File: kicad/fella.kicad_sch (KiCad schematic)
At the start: 4 parts

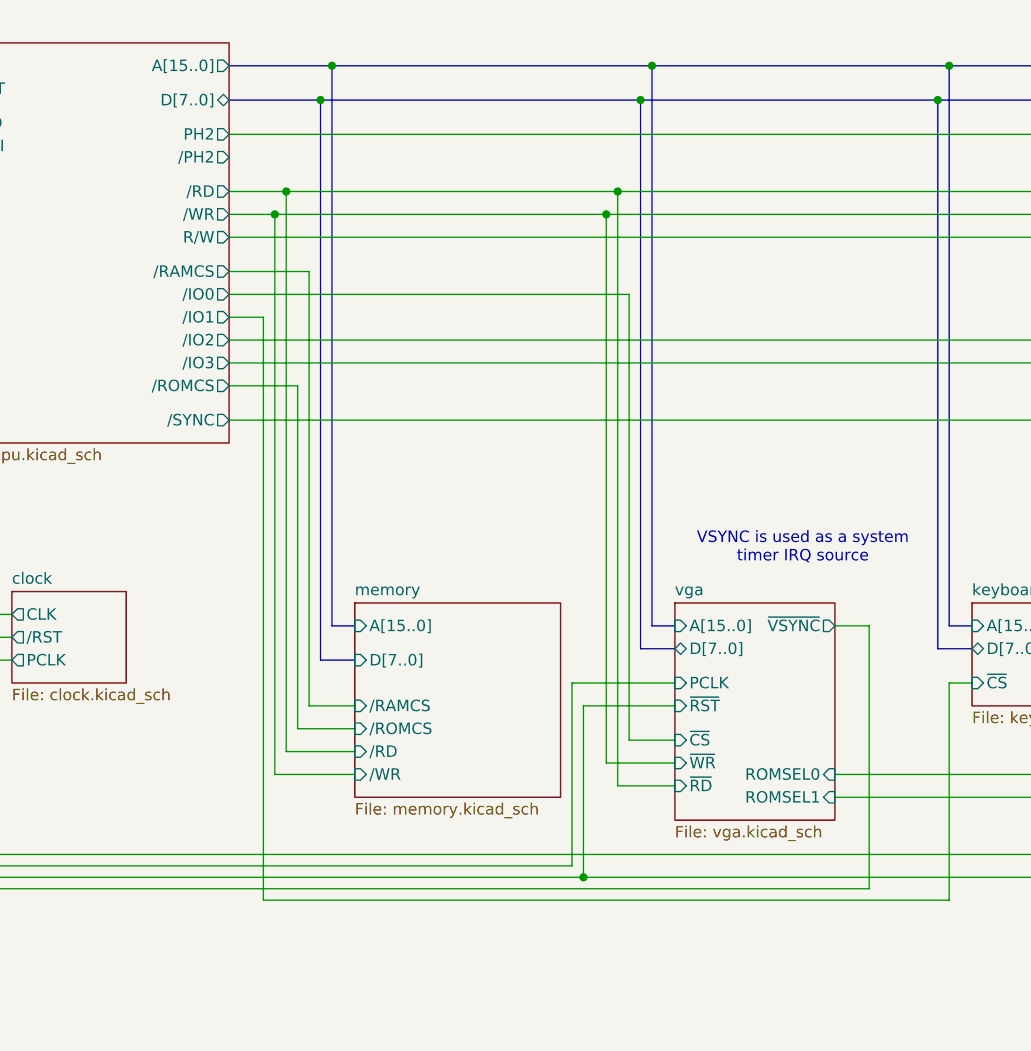
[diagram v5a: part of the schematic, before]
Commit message: hw: Start work on rev B
Changelog:
- fixed IO address decoder (removed /PH2 gating),
- added missing reset circuit capacitor,
- added hardware VGA scrolling,
- removed VGA column register, replaced with address bus,
- fixed values of R5 and R6.
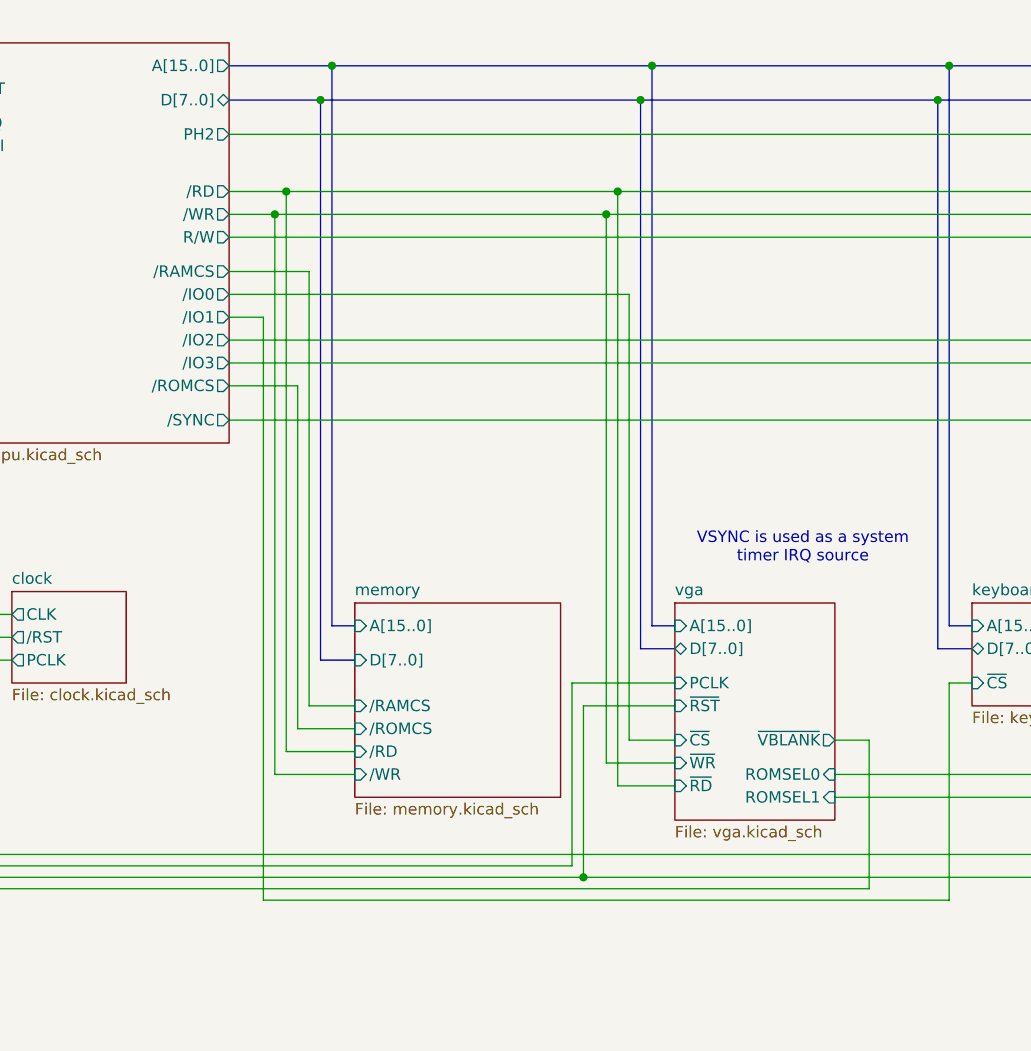
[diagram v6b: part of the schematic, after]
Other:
- sheet cpu ports: added none; removed /PH2
- sheet vga ports: added ~{VBLANK}; removed ~{VSYNC}
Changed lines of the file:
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@@
+	(wire
+		(pts
+			(xy 132.08 132.08) (xy 132.08 115.57)
+		)
+		(stroke
+			(width 0)
+			(type default)
+		)
+	)
 	(wire
 		(pts
@@
 	(wire
 		(pts
-			(xy 128.27 102.87) (xy 132.08 102.87)
-		)
-		(stroke
-			(width 0)
-			(type default)
-		)
-	)
-	(wire
-		(pts
 			(xy 67.31 54.61) (xy 67.31 116.84)
 		)
@@
 		)
 	)
+	(wire
+		(pts
+			(xy 132.08 115.57) (xy 128.27 115.57)
+		)
+		(stroke
+			(width 0)
+			(type default)
+		)
+	)
 	(bus
 		(pts
@@
 		(pts
 			(xy 110.49 102.87) (xy 107.95 102.87)
-		)
-		(stroke
-			(width 0)
-			(type default)
-		)
-	)
-	(wire
-		(pts
-			(xy 132.08 102.87) (xy 132.08 132.08)
 		)
 		(stroke
@@
 			)
 		)
-		(pin "~{VSYNC}" output
-			(at 128.27 102.87 0)
-			(effects
-				(font
-					(size 1.27 1.27)
-				)
-				(justify right)
-			)
-		)
 		(pin "ROMSEL1" input
 			(at 128.27 121.92 0)
@@
 		(pin "ROMSEL0" input
 			(at 128.27 119.38 0)
+			(effects
+				(font
+					(size 1.27 1.27)
+				)
+				(justify right)
+			)
+		)
+		(pin "~{VBLANK}" output
+			(at 128.27 115.57 0)
 			(effects
 				(font
@@
 			(effects
 				(font
-					(size 1.27 1.27)
-				)
-				(justify right)
-			)
-		)
-		(pin "{slash}PH2" output
-			(at 60.96 50.8 0)
-			(effects
-				(font

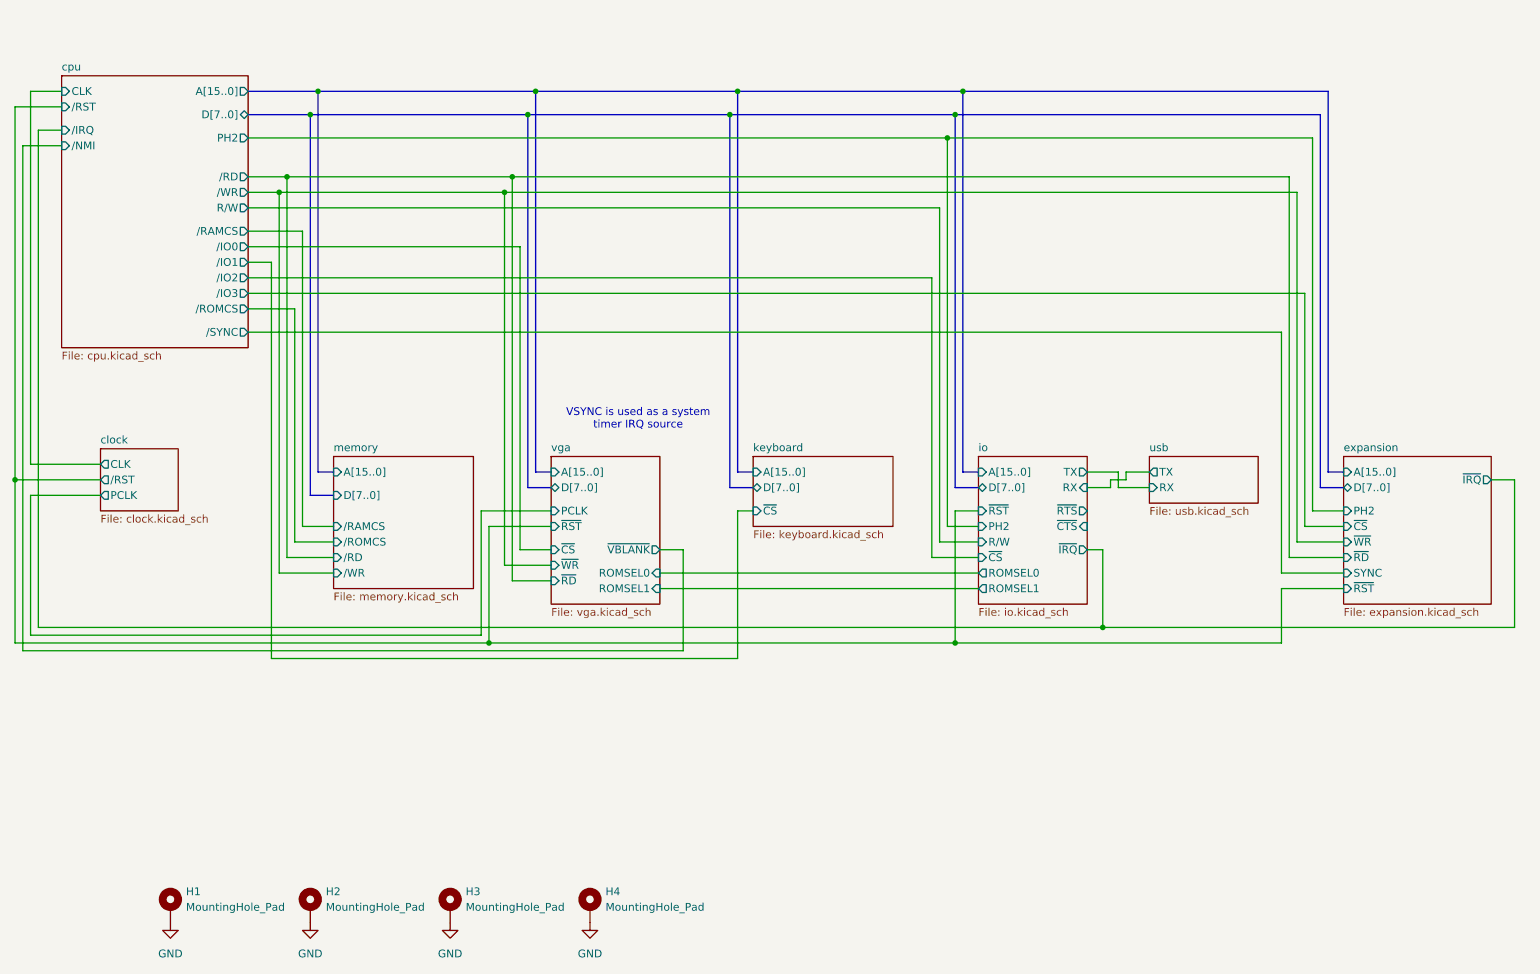
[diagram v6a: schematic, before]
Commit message: hw: revision C
Major changes:
- ROM space has been extended from 16 KiB to 32 KiB
- dynamic RAM option has been removed
- RAM size has been reduced from 32 KiB to 24 KiB
- expansion slot now replaces internal ROM, does not
  have dedicated memory space anymore
- place all I/O within a compactish 8 KiB
- move PH2 gating to /RD and /WR signals
- PCB redo (mechanicaly compatible)
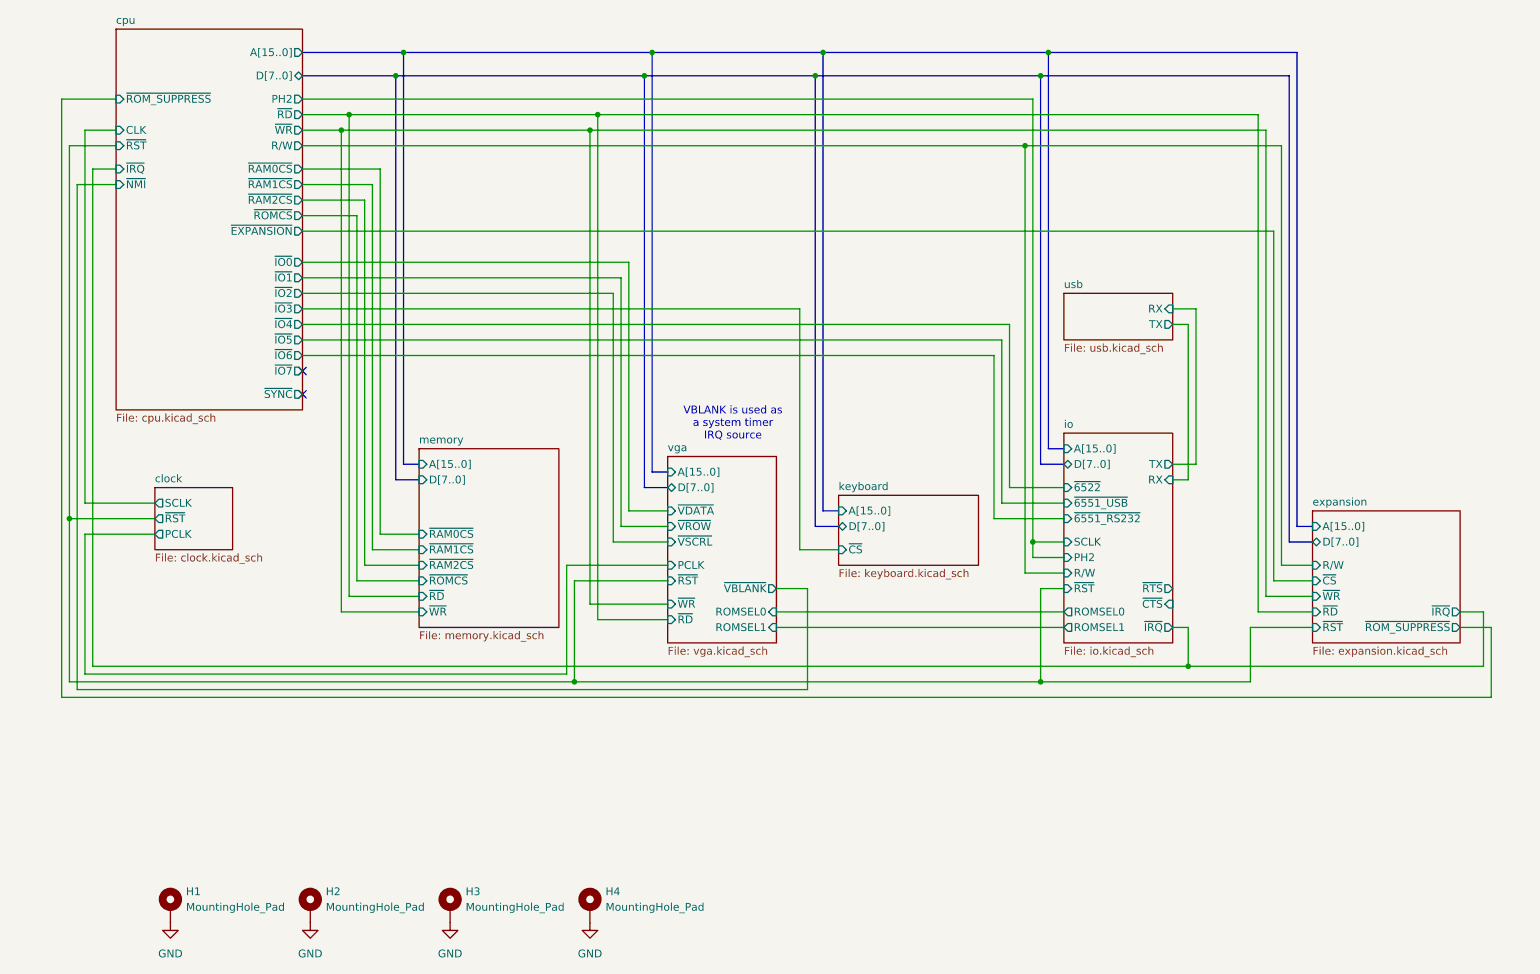
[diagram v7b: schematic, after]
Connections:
- no-connect marks 0 -> 2
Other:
- sheet clock ports: added SCLK, ~{RST}; removed CLK, /RST
- sheet cpu ports: added ~{EXPANSION}, ~{IO0}, ~{IO1}, ~{IO2}, ~{IO3}, ~{IO4}, ~{IO5}, ~{IO6}, ~{IO7}, ~{IRQ}, ~{NMI}, ~{RAM0CS}, ~{RAM1CS}, ~{RAM2CS}, ~{RD}, ~{ROMCS}, ~{ROM_SUPPRESS}, ~{RST}, ~{SYNC}, ~{WR}; removed /IO0, /IO1, /IO2, /IO3, /IRQ, /NMI, /RAMCS, /RD, /ROMCS, /RST, /SYNC, /WR
- sheet expansion ports: added R/W, ~{ROM_SUPPRESS}; removed PH2, SYNC
- sheet io ports: added SCLK, ~{6522}, ~{6551_RS232}, ~{6551_USB}; removed ~{CS}
- sheet memory ports: added ~{RAM0CS}, ~{RAM1CS}, ~{RAM2CS}, ~{RD}, ~{ROMCS}, ~{WR}; removed /RAMCS, /RD, /ROMCS, /WR
- sheet vga ports: added ~{VDATA}, ~{VROW}, ~{VSCRL}; removed ~{CS}
- note added: "VBLANK is used as a system timer IRQ source"
- note removed: "VSYNC is used as a system timer IRQ source"

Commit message: hw: rev D - replace DB25 connector footprint with available one
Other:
- company: (none) -> A.K.
- title: (none) -> FellaPC
